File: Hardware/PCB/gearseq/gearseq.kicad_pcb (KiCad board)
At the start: 2 copper layers, 205 x 165 mm, 68 parts, among them J1 AudioJack2_SwitchT, J10 AudioJack2, J11 AudioJack2, J12 Conn_01x11, J2 AudioJack2_SwitchT, J3 AudioJack2, J4 AudioJack2, J5 Synth_power_2x5, J6 AudioJack2_SwitchT, J7 AudioJack2_SwitchT, J8 Conn_01x12, J9 Conn_01x04, U1 MCP6002-xP, U2 L78L05_TO92

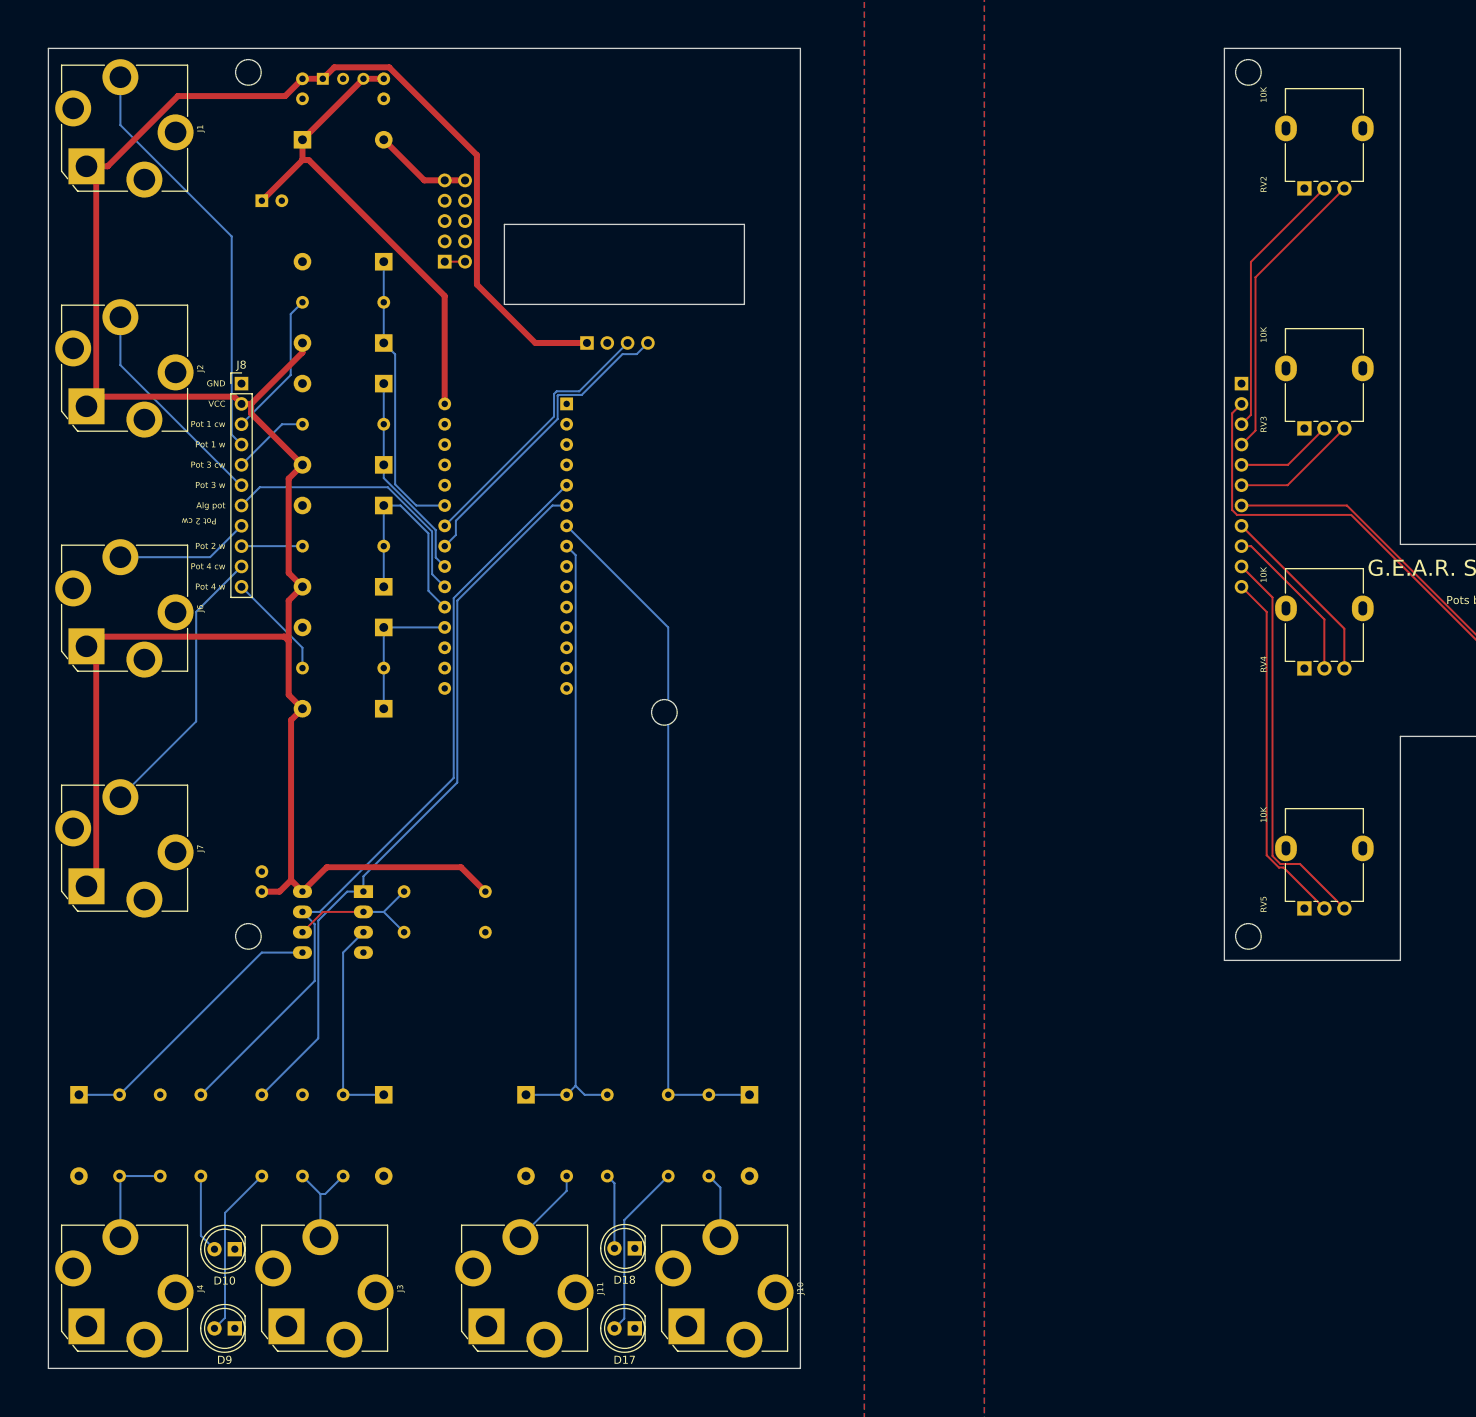
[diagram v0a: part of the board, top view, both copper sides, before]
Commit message: Fix up sketch, add push buttons
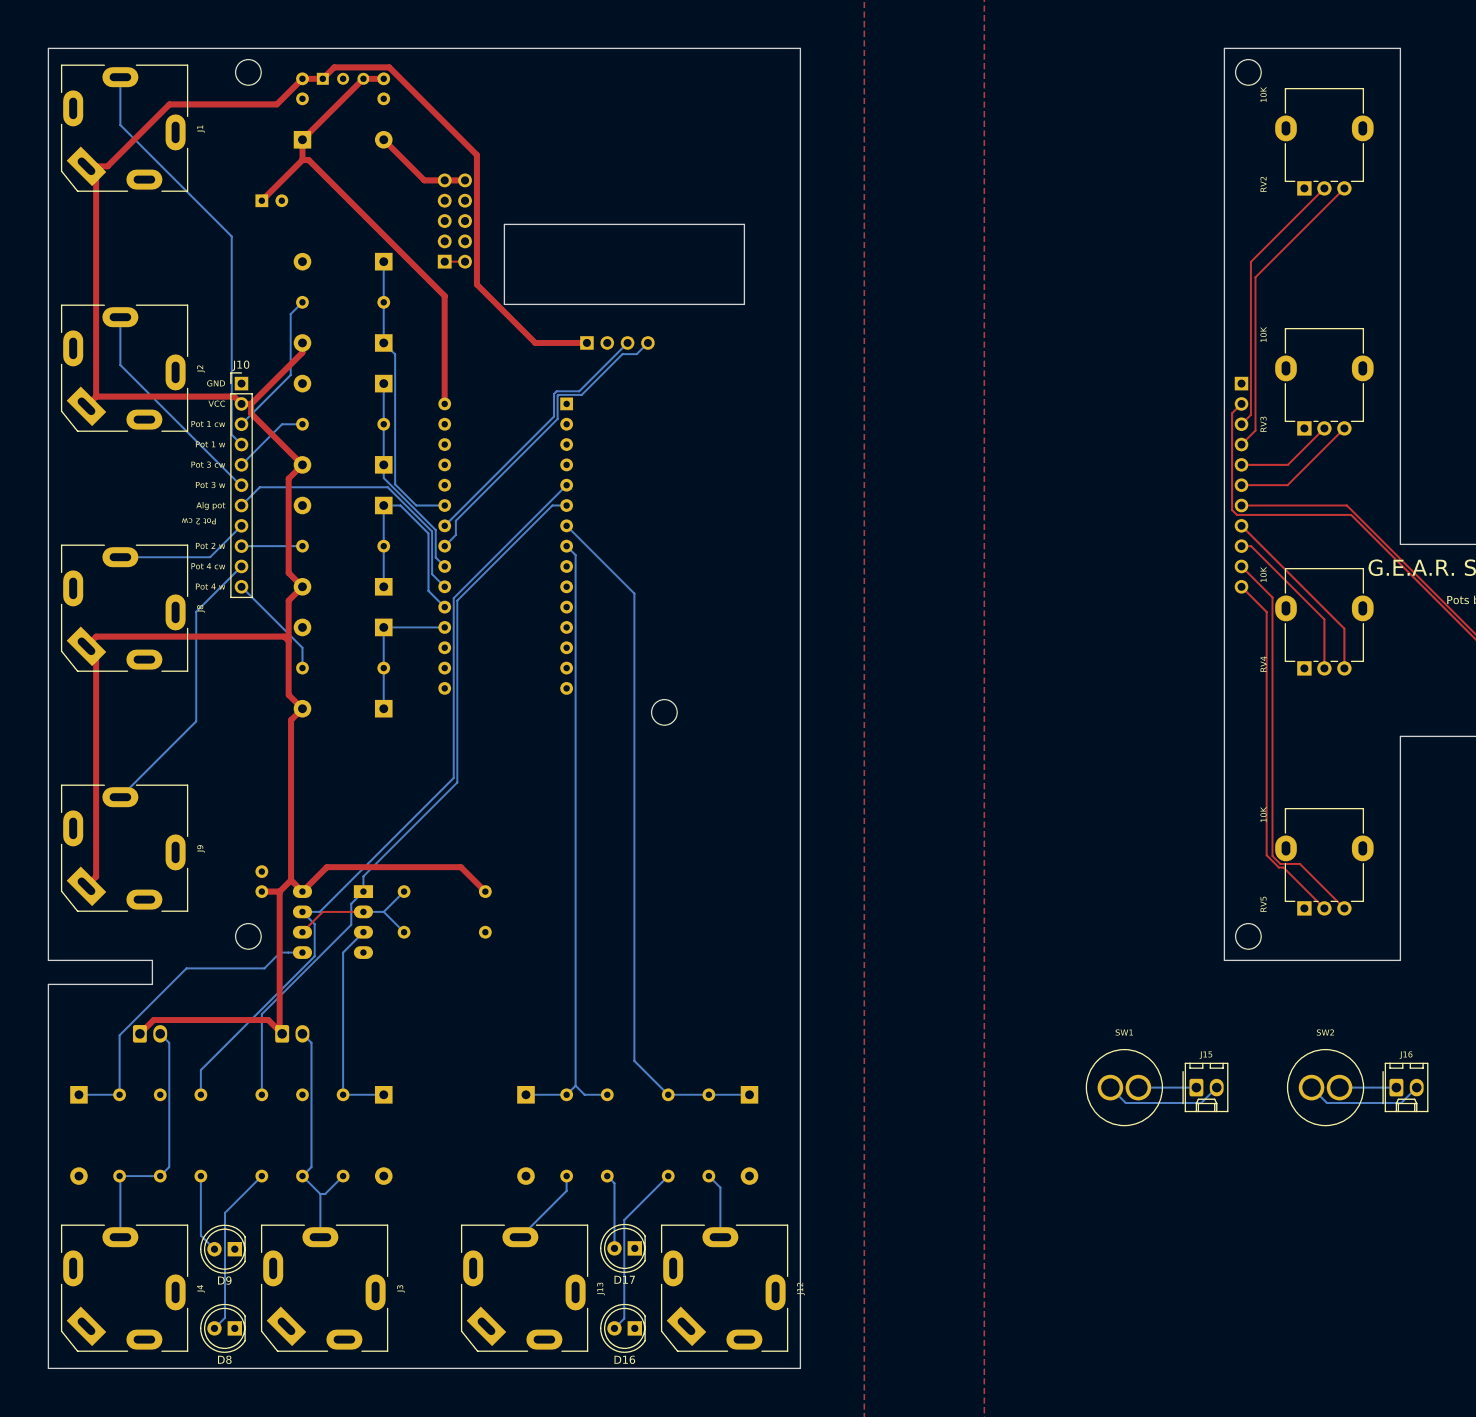
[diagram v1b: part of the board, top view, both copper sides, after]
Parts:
- added J15: 2_pin_Molex_connector, ao_tht:Molex_KK-254_AE-6410-02A_1x02_P2.54mm_Vertical, F.Cu at (169.5, 151.9)
- added J16: 2_pin_Molex_connector, ao_tht:Molex_KK-254_AE-6410-02A_1x02_P2.54mm_Vertical, F.Cu at (194.5, 151.9)
- added J6: 2_pin_Molex_header, ao_tht:Molex_KK-254_AE-6410-02A_1x02_P2.54mm_Vertical, B.Cu at (55.2, 145.2)
- added J7: 2_pin_Molex_header, ao_tht:Molex_KK-254_AE-6410-02A_1x02_P2.54mm_Vertical, B.Cu at (37.4, 145.2)
- added SW1: SW_Push, ao_tht:Push_button_A-5050, F.Cu at (160.5, 151.9)
- added SW2: SW_Push, ao_tht:Push_button_A-5050, F.Cu at (185.6, 151.9)
- J1, J2, J3, J4: footprint ao_tht:Jack_6.35mm_PJ_629HAN -> ao_tht:Jack_6.35mm_PJ_629HAN_slots
- J12: renamed from J10; footprint ao_tht:Jack_6.35mm_PJ_629HAN -> ao_tht:Jack_6.35mm_PJ_629HAN_slots
- J13: renamed from J11; footprint ao_tht:Jack_6.35mm_PJ_629HAN -> ao_tht:Jack_6.35mm_PJ_629HAN_slots
- J8: renamed from J6; footprint ao_tht:Jack_6.35mm_PJ_629HAN -> ao_tht:Jack_6.35mm_PJ_629HAN_slots
- J9: renamed from J7; footprint ao_tht:Jack_6.35mm_PJ_629HAN -> ao_tht:Jack_6.35mm_PJ_629HAN_slots
- renumbered C3 to C2, C4 to C3, C5 to C4, D11 to D10, D12 to D11, D13 to D12, D14 to D13, D15 to D14, D16 to D15, D17 to D16, D18 to D17, D5 to D4, D6 to D5, D7 to D6, D8 to D7, D9 to D8, D10 to D9, H5 to H4, H6 to H5, H7 to H6, J8 to J10, J9 to J11, J12 to J14
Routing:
- net +5V: track 306.8 -> 343.9 mm
- net /RESET_J: track 12.3 -> 31.0 mm
- net /CLK_IN_J: track 12.8 -> 31.5 mm
- net Net-(J15-Pad2): track 0.00 -> 14.9 mm
- net Net-(J16-Pad2): track 0.00 -> 14.7 mm
- net Net-(J15-Pad1): track 0.00 -> 7.25 mm
- net Net-(J16-Pad1): track 0.00 -> 7.10 mm
- net Net-(D2-Pad1): track 35.3 -> 39.7 mm
- net RESET: track 91.7 -> 90.5 mm
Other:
- outline, holes or cut-outs redrawn
- board text added: "Reset button"
- board text added: "Step button"

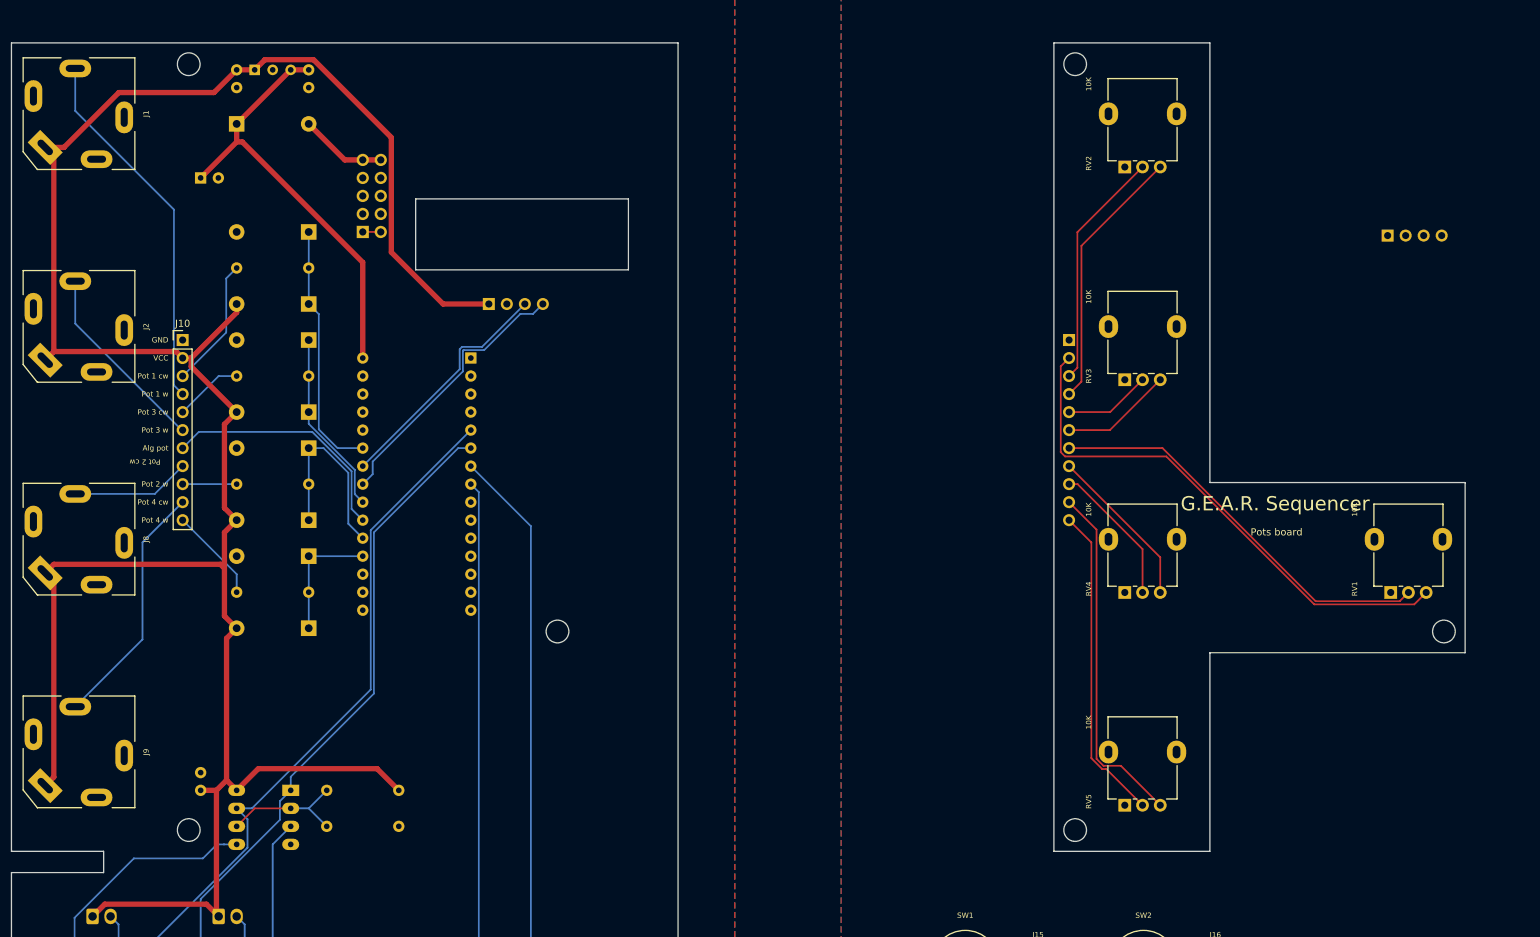
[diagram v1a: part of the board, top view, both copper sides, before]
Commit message: Add 15 mm pot option; BOM
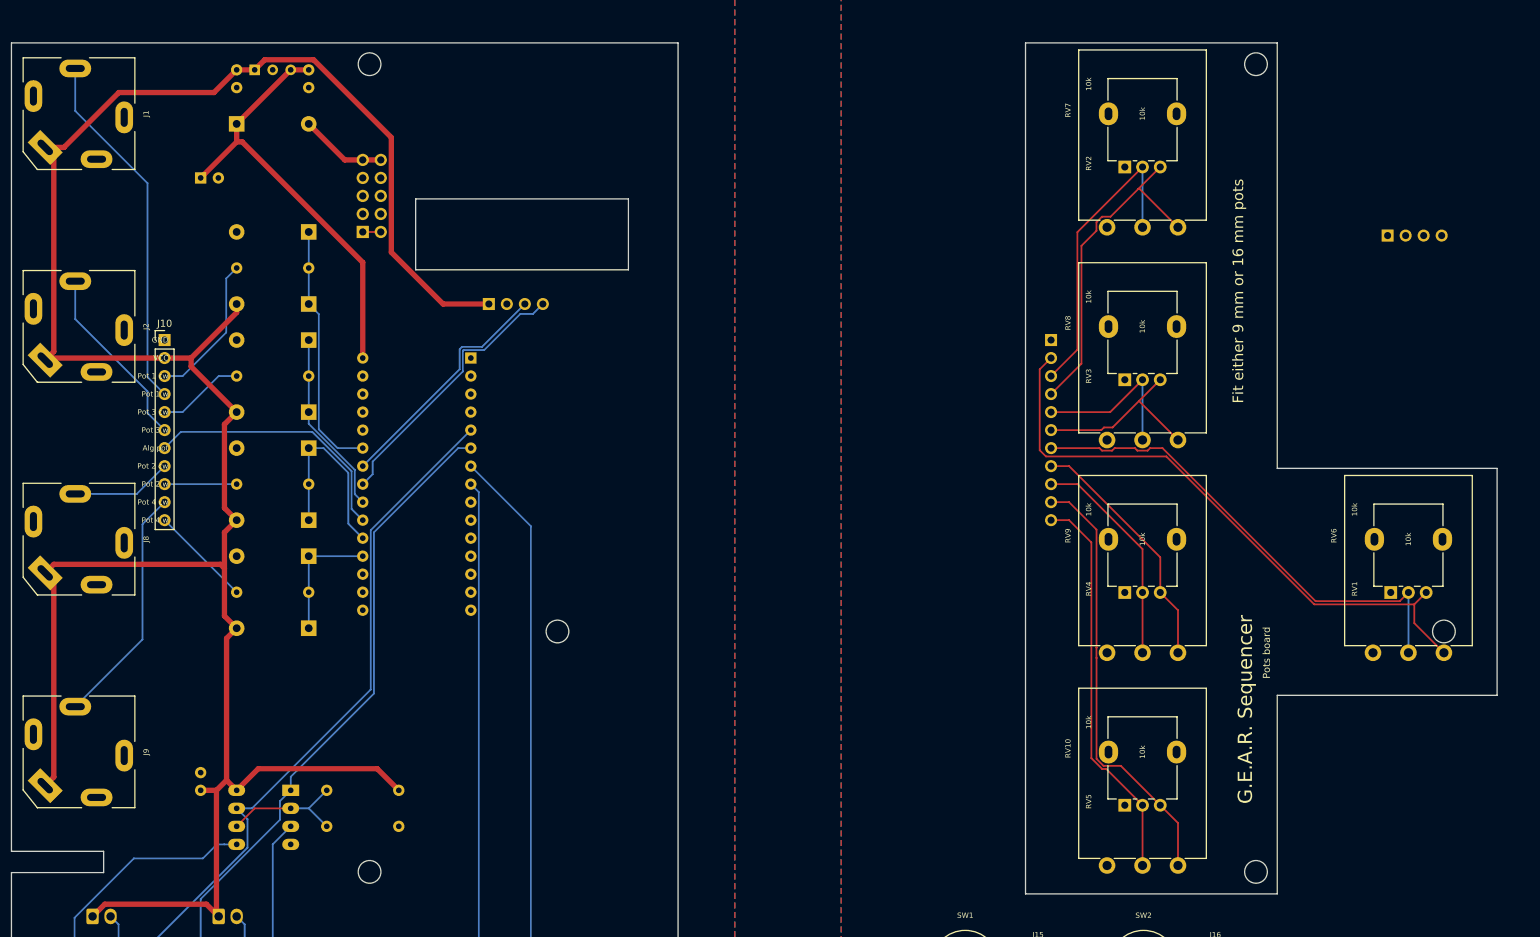
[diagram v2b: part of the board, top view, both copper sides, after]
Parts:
- added RV10: 10k, ao_tht:Potentiometer_Alpha_16mm_Single_Vertical, F.Cu at (185.5, 122.0)
- added RV6: 10k, ao_tht:Potentiometer_Alpha_16mm_Single_Vertical, F.Cu at (223.0, 92.0)
- added RV7: 10k, ao_tht:Potentiometer_Alpha_16mm_Single_Vertical, F.Cu at (185.5, 32.0)
- added RV8: 10k, ao_tht:Potentiometer_Alpha_16mm_Single_Vertical, F.Cu at (185.5, 62.0)
- added RV9: 10k, ao_tht:Potentiometer_Alpha_16mm_Single_Vertical, F.Cu at (185.5, 92.0)
- J10: value Conn_01x12 -> Conn_01x11
- RV1, RV2, RV3, RV4, RV5: value 10K -> 10k
- moved H3 26.2 mm to (76.5, 138.9)
- moved H6 26.2 mm to (201.5, 138.9)
- moved H1 25.5 mm to (76.5, 25.0)
- moved H4 25.5 mm to (201.5, 25.0)
- moved J10 2.54 mm to (47.6, 63.9)
- moved J14 2.54 mm to (172.6, 63.9)
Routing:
- net POT_4_CW_P: track 49.5 -> 61.6 mm
- net POT_3_CW_P: track 23.1 -> 35.2 mm
- net POT_ALG_P: track 57.3 -> 68.9 mm
- net /Panel PCB/VCC: track 74.9 -> 86.4 mm
- net POT_4_W_P: track 44.8 -> 55.9 mm
- net POT_3_W_P: track 20.3 -> 31.3 mm
- net POT_2_W_P: track 12.2 -> 23.3 mm
- net POT_2_CW_P: track 15.8 -> 26.1 mm
- net POT_1_CW_P: track 37.3 -> 46.9 mm
- net POT_1_W_P: track 33.8 -> 43.3 mm
- net POT_3_W: track 7.62 -> 10.2 mm
- net POT_3_CW: track 16.8 -> 14.2 mm
- net POT_2_W: track 9.72 -> 12.3 mm
- net POT_1_W: track 18.4 -> 20.9 mm
- net POT_ALG: track 34.6 -> 37.2 mm
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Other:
- board size 205 x 165 mm -> 209.5 x 165 mm
- board text added: "Fit either 9 mm or 16 mm pots"

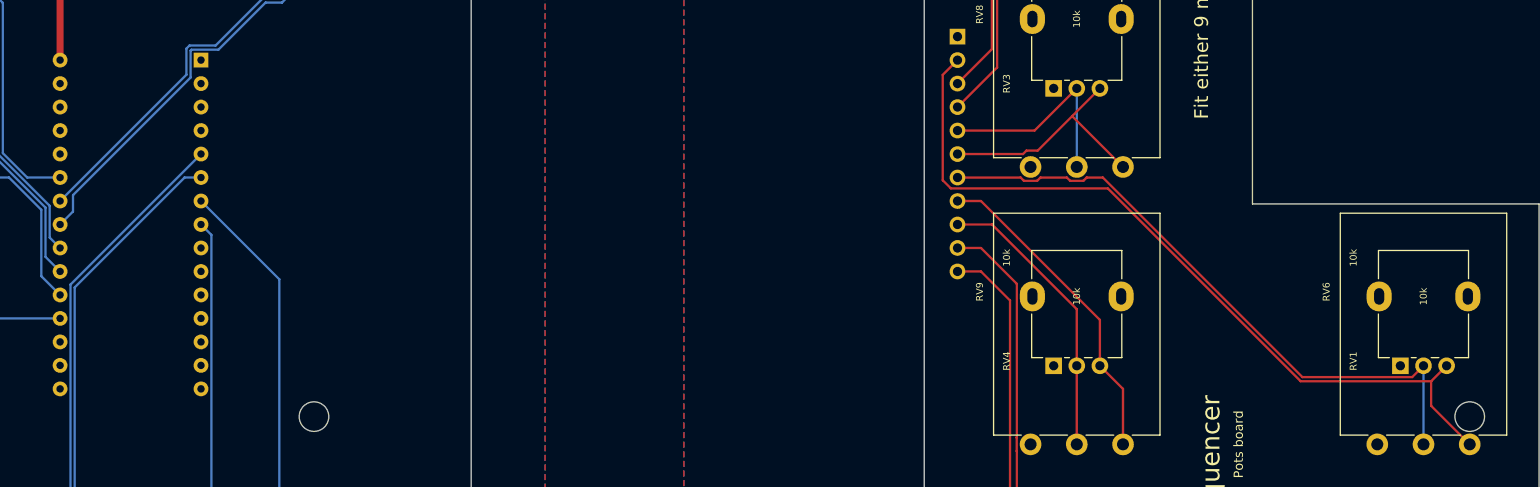
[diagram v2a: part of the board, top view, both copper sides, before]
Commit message: Use ao_symbols
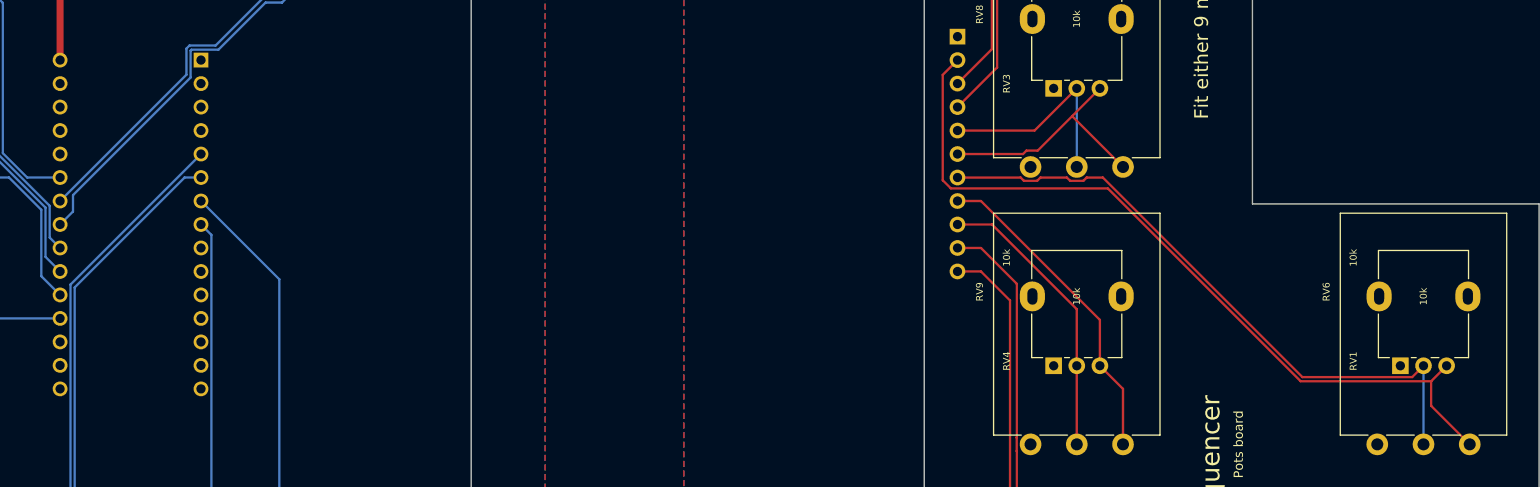
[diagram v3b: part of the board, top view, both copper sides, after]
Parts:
- removed H2, H5: MountingHole, ao_tht:MountingHole_3.2mm_M3
- A1: footprint ao_tht:Arduino_Nano -> Module:Arduino_Nano
- D16, D17, D9: value LED -> LED_green
- D8: value LED -> LED_red
- SW1: value SW_Push -> SW_Push_black
- SW2: value SW_Push -> SW_Push_red
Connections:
- net /Panel PCB/VCC renamed +5V_1
